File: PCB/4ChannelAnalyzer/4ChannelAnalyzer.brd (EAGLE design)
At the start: 100 x 80 mm, 0 parts

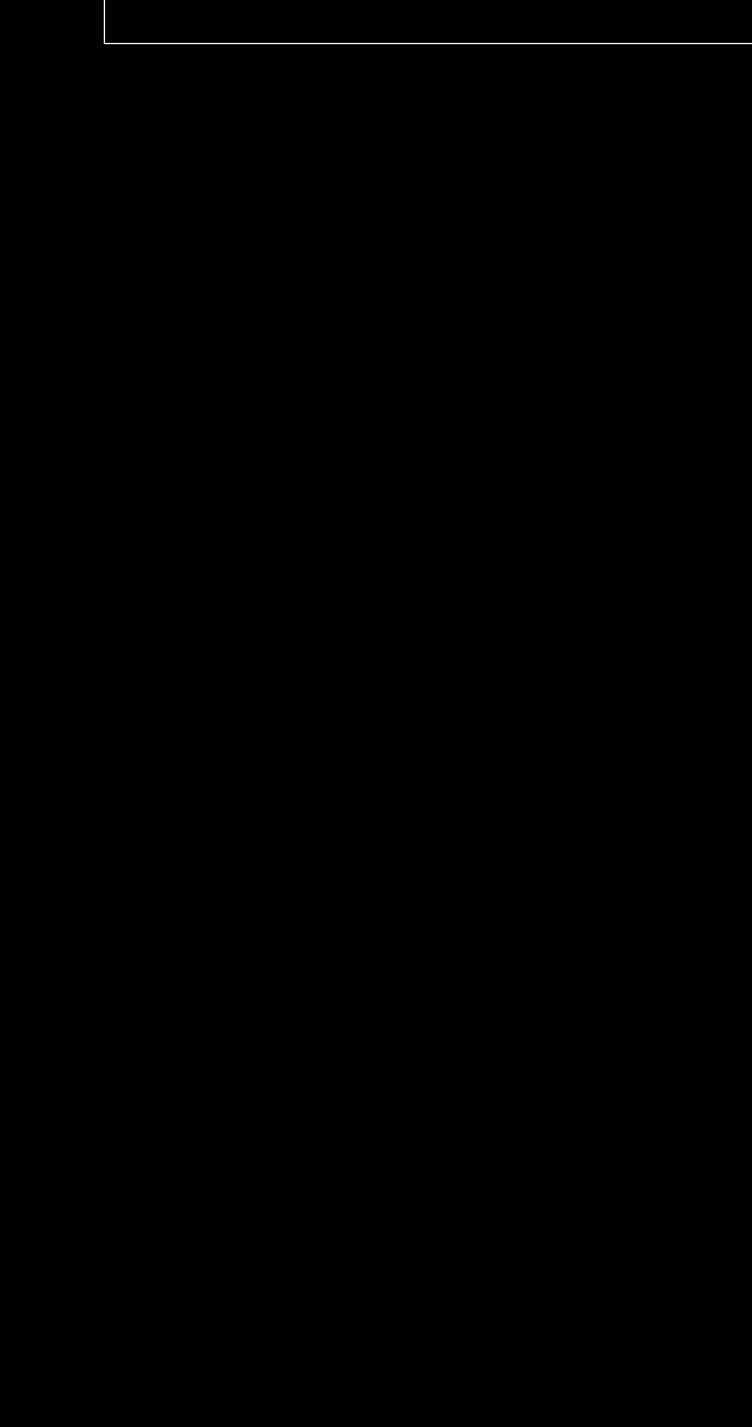
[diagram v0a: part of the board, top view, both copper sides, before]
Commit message: Added components to the PCB design
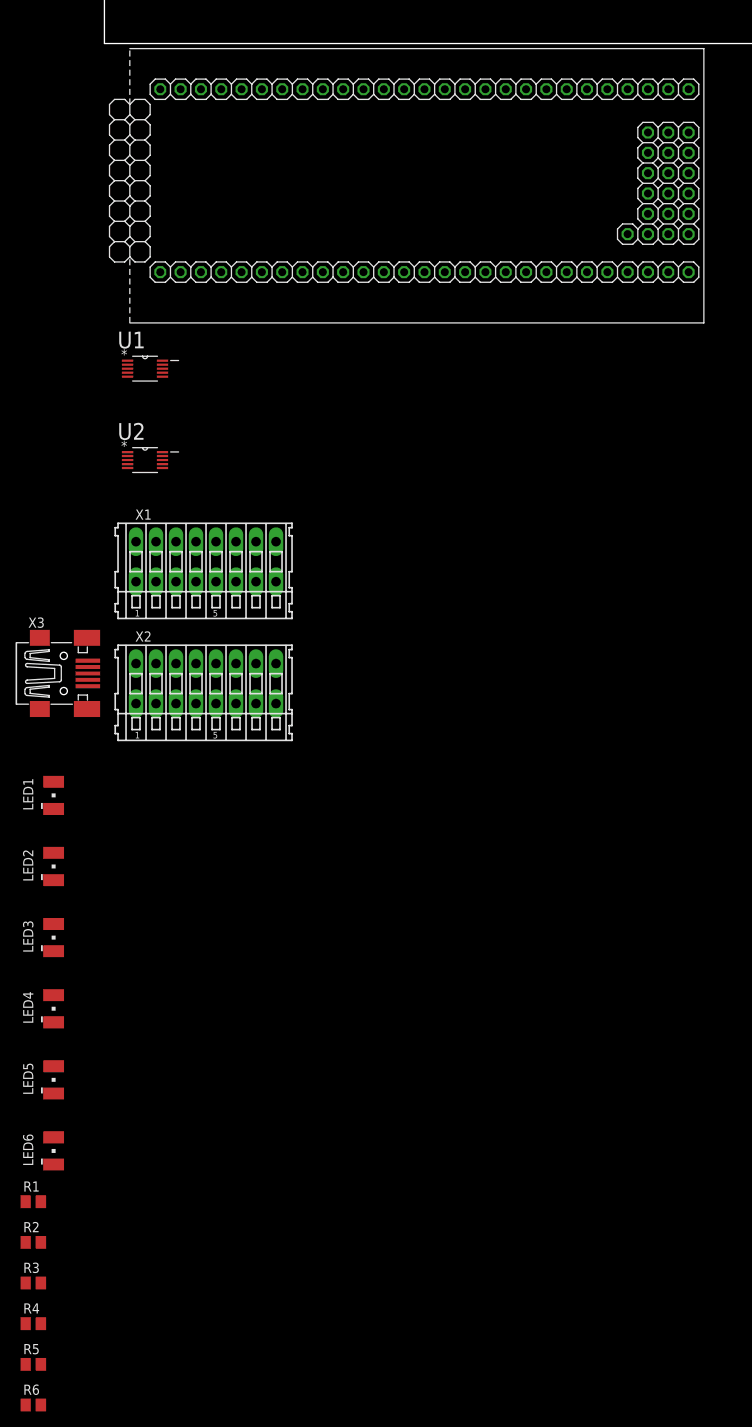
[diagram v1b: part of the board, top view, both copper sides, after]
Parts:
- added LED1, LED2, LED3, LED4, LED5, LED6: LG_T679-E1F1-1, led:PLCC2
- added LPC1: (no value), LPCXpresso_LPC1769:LPCXPRESSO_LPC1769
- added R1, R2, R3, R4, R5, R6: (no value), rcl:M2012
- added U1, U2: ADS1015IDGST, ADS1015:SOP50P490X110-10N
- added X1, X2: (no value), con-wago255:233-108
- added X3: MINI-USB-32005-301, con-cypressindustries:32005-301
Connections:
- new net VDD: U1.8, U2.8

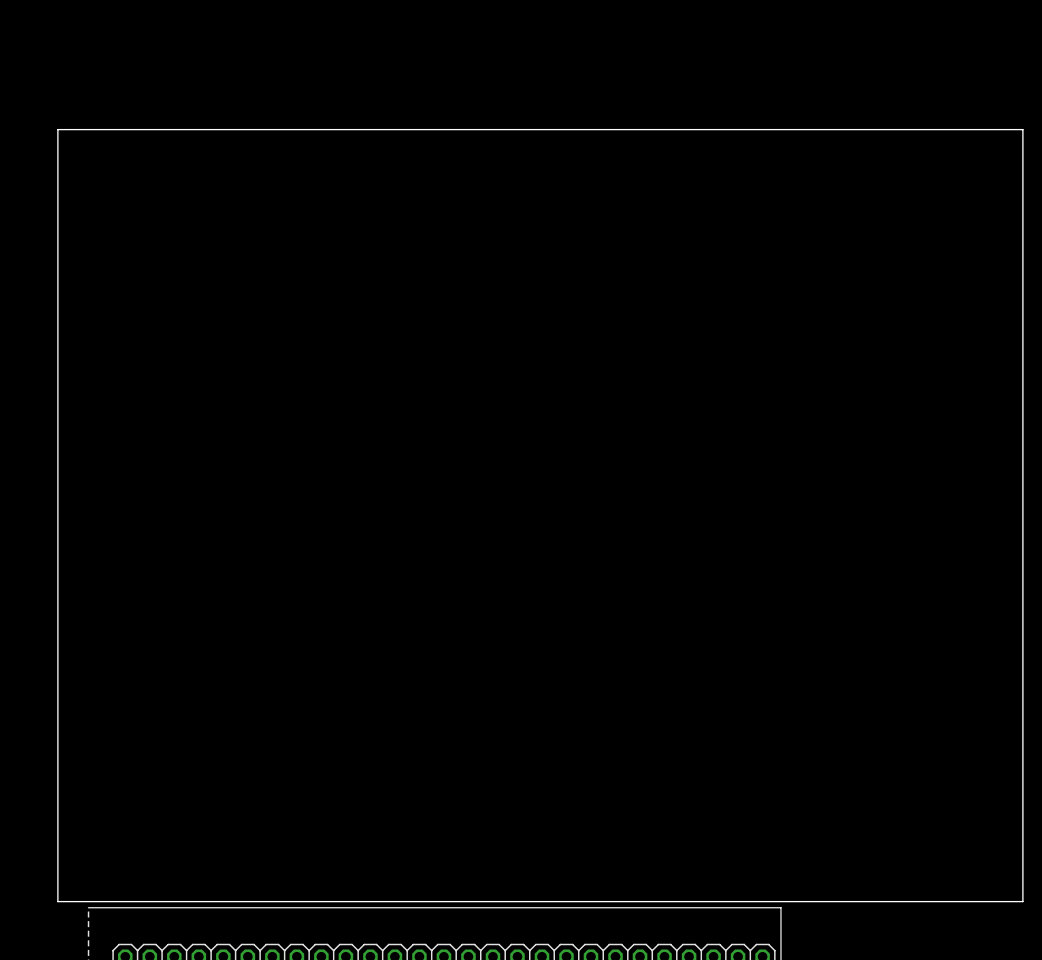
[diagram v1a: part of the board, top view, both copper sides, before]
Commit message: Marking dimension of the PCB board. (Milling line)
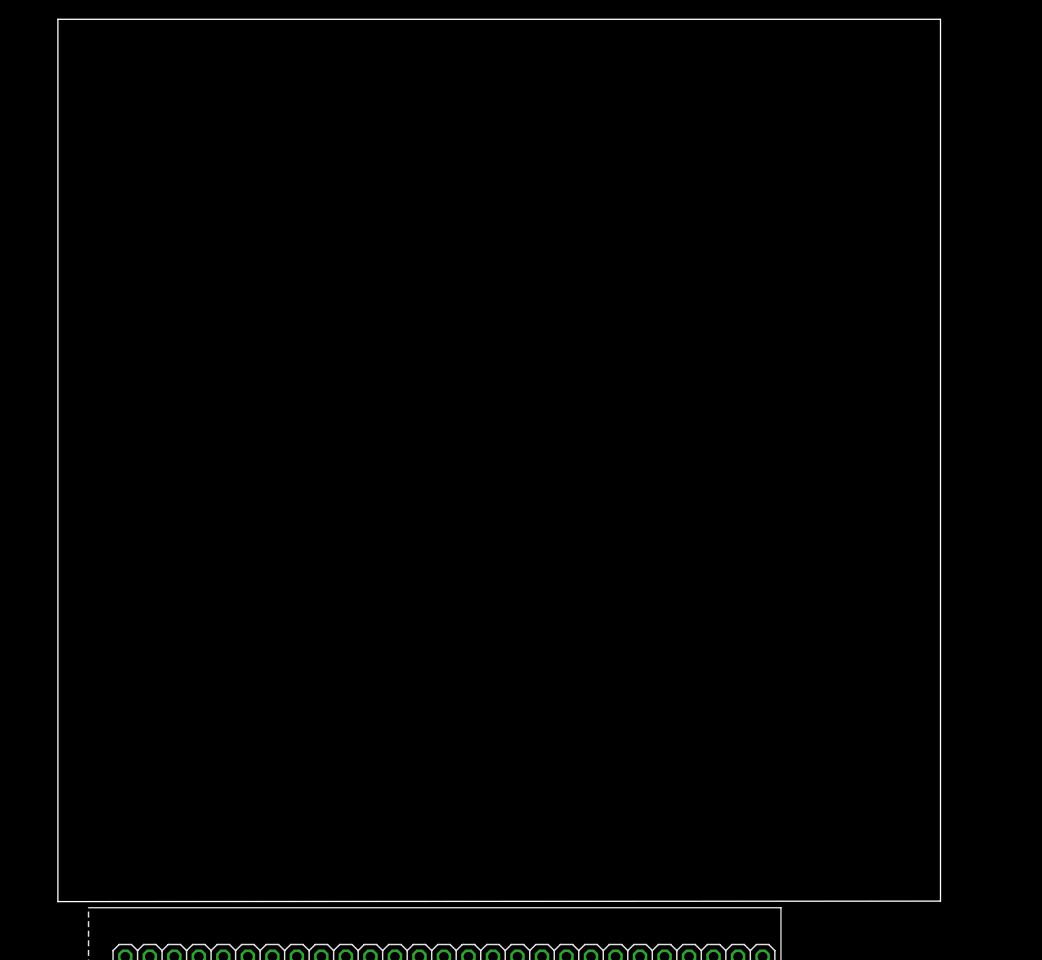
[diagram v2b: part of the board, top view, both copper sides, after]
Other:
- board size 100 x 80 mm -> 91.5 x 91.4 mm
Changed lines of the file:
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@@
 <layer number="44" name="Drills" color="7" fill="1" visible="no" active="yes"/>
 <layer number="45" name="Holes" color="7" fill="1" visible="no" active="yes"/>
-<layer number="46" name="Milling" color="3" fill="1" visible="no" active="yes"/>
+<layer number="46" name="Milling" color="3" fill="1" visible="yes" active="yes"/>
 <layer number="47" name="Measures" color="7" fill="1" visible="no" active="yes"/>
 <layer number="48" name="Document" color="7" fill="1" visible="yes" active="yes"/>
@@
 <board>
 <plain>
-<wire x1="0" y1="0" x2="100" y2="0" width="0" layer="20"/>
-<wire x1="100" y1="0" x2="100" y2="80" width="0" layer="20"/>
-<wire x1="100" y1="80" x2="0" y2="80" width="0" layer="20"/>
-<wire x1="0" y1="80" x2="0" y2="0" width="0" layer="20"/>
+<wire x1="0" y1="0" x2="91.46" y2="0.05" width="0" layer="46"/>
+<wire x1="91.46" y1="0.05" x2="91.46" y2="91.43" width="0" layer="46"/>
+<wire x1="91.46" y1="91.43" x2="0" y2="91.43" width="0" layer="46"/>
+<wire x1="0" y1="91.43" x2="0" y2="0" width="0" layer="46"/>
+<dimension x1="0" y1="80" x2="91.44" y2="80.01" x3="45.718334375" y3="95.245" textsize="1.778" layer="20"/>
+<dimension x1="0" y1="0" x2="0" y2="91.44" x3="-3.81" y3="45.72" textsize="1.778" layer="20" width="0.26"/>
 </plain>
 <attributes>

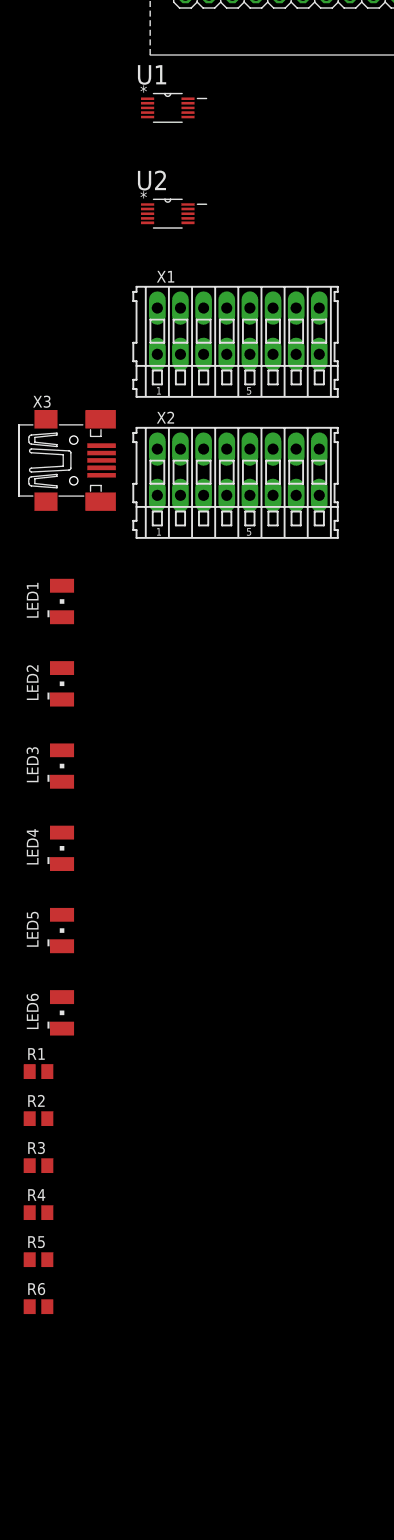
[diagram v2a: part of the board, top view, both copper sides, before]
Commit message: Wiring ADCs with connectors and LED.
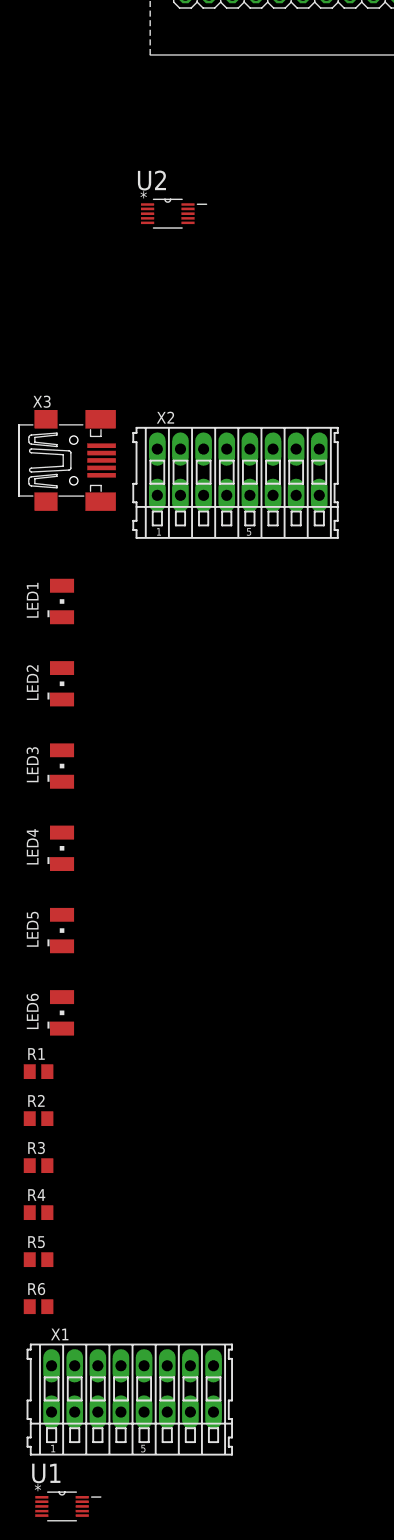
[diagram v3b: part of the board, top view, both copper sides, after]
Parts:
- moved U1 151.6 mm to (-6.35, -191.8)
- moved X1 114.9 mm to (1.27, -179.1)
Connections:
- new net GND: LED1.C, LED2.C, LED3.C, LED4.C, LED5.C, LED6.C, U1.3, U2.3, X1.A2, X1.A4, X1.A6, X1.A8, X2.A2, X2.A4, X2.A6, X2.A8
- new net N$1: U1.4, X1.A1
- new net N$10: U2.5, X2.A3
- new net N$11: U2.6, X2.A5
- new net N$12: U2.7, X2.A7
- new net N$13: U1.6, X1.A5
- new net N$14: U1.7, X1.A7
- new net N$2: LED4.A, R1.1
- new net N$3: LED1.A, R2.1
- new net N$4: LED2.A, R3.1
- new net N$5: LED3.A, R4.1
- new net N$6: LED5.A, R5.1
- new net N$7: LED6.A, R6.1
- new net N$8: U1.5, X1.A3
- new net N$9: U2.4, X2.A1
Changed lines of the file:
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@@
 <elements>
 <element name="LPC1" library="LPCXpresso_LPC1769" package="LPCXPRESSO_LPC1769" value="" x="27.94" y="-17.78"/>
-<element name="U1" library="ADS1015" package="SOP50P490X110-10N" value="ADS1015IDGST" x="5.08" y="-40.64">
-<attribute name="PACKAGE" value="MSOP-10" x="5.08" y="-40.64" size="1.778" layer="27" display="off"/>
-<attribute name="OC_NEWARK" value="35R0211" x="5.08" y="-40.64" size="1.778" layer="27" display="off"/>
-<attribute name="MPN" value="ADS1015IDGST" x="5.08" y="-40.64" size="1.778" layer="27" display="off"/>
-<attribute name="SUPPLIER" value="Texas Instruments" x="5.08" y="-40.64" size="1.778" layer="27" display="off"/>
-<attribute name="OC_FARNELL" value="1778211" x="5.08" y="-40.64" size="1.778" layer="27" display="off"/>
-</element>
 <element name="U2" library="ADS1015" package="SOP50P490X110-10N" value="ADS1015IDGST" x="5.08" y="-52.07">
 <attribute name="PACKAGE" value="MSOP-10" x="5.08" y="-52.07" size="1.778" layer="27" display="off"/>
@@
 <attribute name="SUPPLIER" value="Texas Instruments" x="5.08" y="-52.07" size="1.778" layer="27" display="off"/>
 <attribute name="OC_FARNELL" value="1778211" x="5.08" y="-52.07" size="1.778" layer="27" display="off"/>
-</element>
-<element name="X1" library="con-wago255" package="233-108" value="" x="12.7" y="-64.77">
-<attribute name="OC_NEWARK" value="28K9050" x="12.7" y="-64.77" size="1.778" layer="27" display="off"/>
-<attribute name="MPN" value="233-108" x="12.7" y="-64.77" size="1.778" layer="27" display="off"/>
-<attribute name="MF" value="" x="12.7" y="-64.77" size="1.778" layer="27" display="off"/>
-<attribute name="OC_FARNELL" value="unknown" x="12.7" y="-64.77" size="1.778" layer="27" display="off"/>
 </element>
 <element name="X2" library="con-wago255" package="233-108" value="" x="12.7" y="-80.01">
@@
 <element name="R5" library="rcl" package="M2012" value="" x="-8.89" y="-165.1"/>
 <element name="R6" library="rcl" package="M2012" value="" x="-8.89" y="-170.18"/>
+<element name="U1" library="ADS1015" package="SOP50P490X110-10N" value="ADS1015IDGST" x="-6.35" y="-191.77">
+<attribute name="PACKAGE" value="MSOP-10" x="-6.35" y="-176.53" size="1.778" layer="27" display="off"/>
+<attribute name="OC_NEWARK" value="35R0211" x="-6.35" y="-176.53" size="1.778" layer="27" display="off"/>
+<attribute name="MPN" value="ADS1015IDGST" x="-6.35" y="-176.53" size="1.778" layer="27" display="off"/>
+<attribute name="SUPPLIER" value="Texas Instruments" x="-6.35" y="-176.53" size="1.778" layer="27" display="off"/>
+<attribute name="OC_FARNELL" value="1778211" x="-6.35" y="-176.53" size="1.778" layer="27" display="off"/>
+</element>
+<element name="X1" library="con-wago255" package="233-108" value="" x="1.27" y="-179.07">
+<attribute name="OC_NEWARK" value="28K9050" x="1.27" y="-189.23" size="1.778" layer="27" display="off"/>
+<attribute name="MPN" value="233-108" x="1.27" y="-189.23" size="1.778" layer="27" display="off"/>
+<attribute name="MF" value="" x="1.27" y="-189.23" size="1.778" layer="27" display="off"/>
+<attribute name="OC_FARNELL" value="unknown" x="1.27" y="-189.23" size="1.778" layer="27" display="off"/>
+</element>
 </elements>
 <signals>
 <signal name="VDD">
+<contactref element="U2" pad="8"/>
 <contactref element="U1" pad="8"/>
-<contactref element="U2" pad="8"/>
-<wire x1="7.2644" y1="-40.64" x2="7.2644" y2="-52.07" width="0" layer="19" extent="1-1"/>
+<wire x1="7.2644" y1="-52.07" x2="-4.1656" y2="-191.77" width="0" layer="19" extent="1-1"/>
+</signal>
+<signal name="GND">
+<contactref element="LED4" pad="C"/>
+<contactref element="LED6" pad="C"/>
+<contactref element="LED5" pad="C"/>
+<contactref element="LED3" pad="C"/>
+<contactref element="LED2" pad="C"/>
+<contactref element="LED1" pad="C"/>
+<contactref element="U2" pad="3"/>
+<contactref element="X2" pad="A8"/>
+<contactref element="X2" pad="A6"/>
+<contactref element="X2" pad="A4"/>
+<contactref element="X2" pad="A2"/>
+<contactref element="U1" pad="3"/>
+<contactref element="X1" pad="A8"/>
+<contactref element="X1" pad="A6"/>
+<contactref element="X1" pad="A4"/>
+<contactref element="X1" pad="A2"/>
+<wire x1="-4.98" y1="-176.57" x2="-8.5344" y2="-191.77" width="0" layer="19" extent="1-1"/>
+<wire x1="0.02" y1="-176.57" x2="-4.98" y2="-176.57" width="0" layer="19" extent="1-1"/>
+<wire x1="5.02" y1="-176.57" x2="0.02" y2="-176.57" width="0" layer="19" extent="1-1"/>
+<wire x1="10.02" y1="-176.57" x2="5.02" y2="-176.57" width="0" layer="19" extent="1-1"/>
+<wire x1="-6.35" y1="-140.13" x2="-4.98" y2="-176.57" width="0" layer="19" extent="1-1"/>
+<wire x1="-6.35" y1="-131.24" x2="-6.35" y2="-140.13" width="0" layer="19" extent="1-1"/>
+<wire x1="-6.35" y1="-122.35" x2="-6.35" y2="-131.24" width="0" layer="19" extent="1-1"/>
+<wire x1="-6.35" y1="-113.46" x2="-6.35" y2="-122.35" width="0" layer="19" extent="1-1"/>
+<wire x1="-6.35" y1="-104.57" x2="-6.35" y2="-113.46" width="0" layer="19" extent="1-1"/>
+<wire x1="-6.35" y1="-95.68" x2="-6.35" y2="-104.57" width="0" layer="19" extent="1-1"/>
+<wire x1="6.45" y1="-77.51" x2="-6.35" y2="-95.68" width="0" layer="19" extent="1-1"/>
+<wire x1="11.45" y1="-77.51" x2="6.45" y2="-77.51" width="0" layer="19" extent="1-1"/>
+<wire x1="16.45" y1="-77.51" x2="11.45" y2="-77.51" width="0" layer="19" extent="1-1"/>
+<wire x1="21.45" y1="-77.51" x2="16.45" y2="-77.51" width="0" layer="19" extent="1-1"/>
+<wire x1="2.8956" y1="-52.07" x2="6.45" y2="-77.51" width="0" layer="19" extent="1-1"/>
+</signal>
+<signal name="N$2">
+<contactref element="R1" pad="1"/>
+<contactref element="LED4" pad="A"/>
+<wire x1="-6.35" y1="-118.95" x2="-9.84" y2="-144.78" width="0" layer="19" extent="1-1"/>
+</signal>
+<signal name="N$3">
+<contactref element="R2" pad="1"/>
+<contactref element="LED1" pad="A"/>
+<wire x1="-6.35" y1="-92.28" x2="-9.84" y2="-149.86" width="0" layer="19" extent="1-1"/>
+</signal>
+<signal name="N$4">
+<contactref element="R3" pad="1"/>
+<contactref element="LED2" pad="A"/>
+<wire x1="-6.35" y1="-101.17" x2="-9.84" y2="-154.94" width="0" layer="19" extent="1-1"/>
+</signal>
+<signal name="N$5">
+<contactref element="R4" pad="1"/>
+<contactref element="LED3" pad="A"/>
+<wire x1="-6.35" y1="-110.06" x2="-9.84" y2="-160.02" width="0" layer="19" extent="1-1"/>
+</signal>
+<signal name="N$6">
+<contactref element="R5" pad="1"/>
+<contactref element="LED5" pad="A"/>
+<wire x1="-6.35" y1="-127.84" x2="-9.84" y2="-165.1" width="0" layer="19" extent="1-1"/>
+</signal>
+<signal name="N$7">
+<contactref element="R6" pad="1"/>
+<contactref element="LED6" pad="A"/>
+<wire x1="-6.35" y1="-136.73" x2="-9.84" y2="-170.18" width="0" layer="19" extent="1-1"/>
+</signal>
+<signal name="N$9">
+<contactref element="U2" pad="4"/>
+<contactref element="X2" pad="A1"/>
+<wire x1="2.8956" y1="-52.578" x2="3.95" y2="-77.51" width="0" layer="19" extent="1-1"/>
+</signal>
+<signal name="N$10">
+<contactref element="U2" pad="5"/>
+<contactref element="X2" pad="A3"/>
+<wire x1="2.8956" y1="-53.0606" x2="8.95" y2="-77.51" width="0" layer="19" extent="1-1"/>
+</signal>
+<signal name="N$11">
+<contactref element="U2" pad="6"/>
+<contactref element="X2" pad="A5"/>
+<wire x1="7.2644" y1="-53.0606" x2="13.95" y2="-77.51" width="0" layer="19" extent="1-1"/>
+</signal>
+<signal name="N$12">
+<contactref element="U2" pad="7"/>
+<contactref element="X2" pad="A7"/>
+<wire x1="7.2644" y1="-52.578" x2="18.95" y2="-77.51" width="0" layer="19" extent="1-1"/>
+</signal>
+<signal name="N$1">
+<contactref element="U1" pad="4"/>
+<contactref element="X1" pad="A1"/>
+<wire x1="-7.48" y1="-176.57" x2="-8.5344" y2="-192.278" width="0" layer="19" extent="1-1"/>
+</signal>
+<signal name="N$8">
+<contactref element="U1" pad="5"/>
+<contactref element="X1" pad="A3"/>
+<wire x1="-2.48" y1="-176.57" x2="-8.5344" y2="-192.7606" width="0" layer="19" extent="1-1"/>
+</signal>
+<signal name="N$13">
+<contactref element="U1" pad="6"/>
+<contactref element="X1" pad="A5"/>
+<wire x1="2.52" y1="-176.57" x2="-4.1656" y2="-192.7606" width="0" layer="19" extent="1-1"/>
+</signal>
+<signal name="N$14">
+<contactref element="U1" pad="7"/>
+<contactref element="X1" pad="A7"/>
+<wire x1="7.52" y1="-176.57" x2="-4.1656" y2="-192.278" width="0" layer="19" extent="1-1"/>
 </signal>
 </signals>

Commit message: Repositioning components in to PCB design
Repositioning components which are included in to the project
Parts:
- added U3: LM1117MP-3.3, LM1117MP-3.3:SOT230P696X180-4N
- moved R2 229.1 mm to (128.3, 33.7)
- moved R4 229.1 mm to (128.3, 23.5)
- moved R6 229.1 mm to (128.3, 13.3)
- moved R1 229.1 mm to (128.3, 38.7)
- moved R3 229.1 mm to (128.3, 28.6)
- moved R5 229.1 mm to (128.3, 18.4)
- moved U1 223.3 mm to (67.3, 19.1), turned to 90 degrees
- moved LED6 223.2 mm to (148.6, 22.2)
- moved LED5 222.7 mm to (148.6, 30.5)
- moved LED4 221.9 mm to (145.4, 41.3)
- moved LED3 218.1 mm to (139.1, 50.8)
- moved X1 214.7 mm to (82.5, 19.7), turned to 90 degrees
- moved LED2 203.9 mm to (127.6, 50.8)
- moved LED1 190.8 mm to (111.8, 55.9)
- moved X2 171.7 mm to (82.5, 76.8), turned to 90 degrees
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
